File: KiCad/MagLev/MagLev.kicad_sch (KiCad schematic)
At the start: 22 parts, among them Q1 2SD2673, Q2 2SB1708, Q3 2SD2673, Q4 2SB1708, U1 LM324

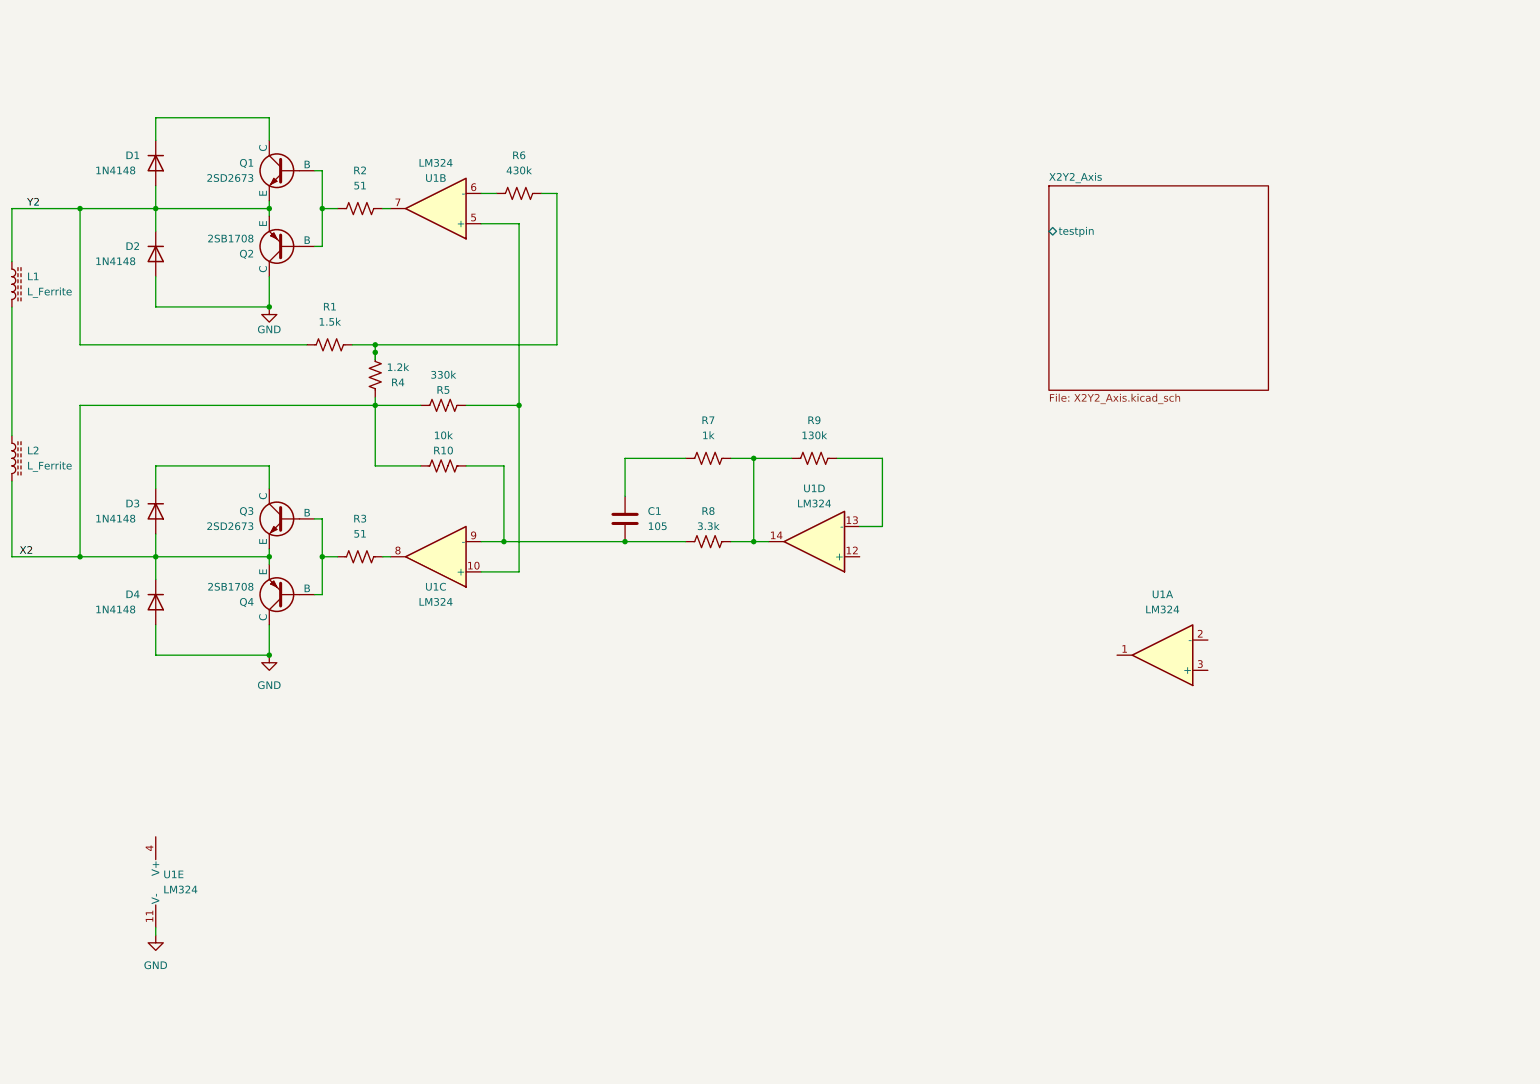
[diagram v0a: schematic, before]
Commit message: Update component names to match ENB schematic.
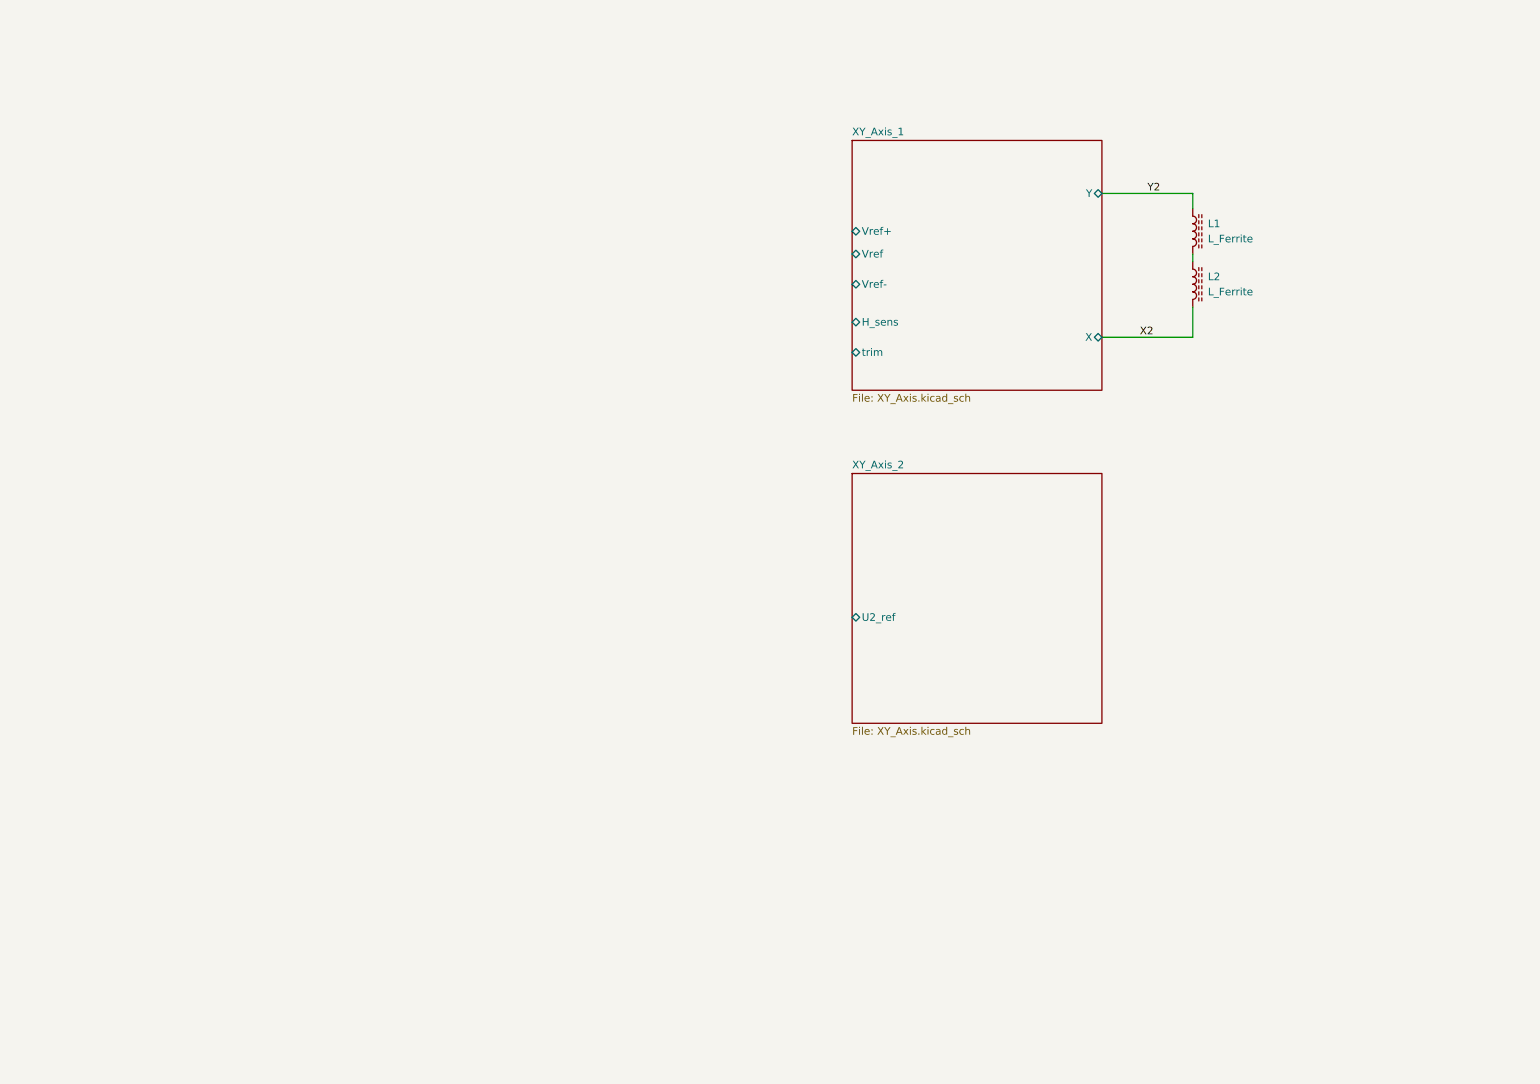
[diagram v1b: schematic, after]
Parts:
- removed C1: 105, symbol Device:C
- removed D1, D2, D3, D4: 1N4148, symbol Device:D
- removed Q1, Q3: 2SD2673, symbol Simulation_SPICE:NPN
- removed Q2, Q4: 2SB1708, symbol Simulation_SPICE:PNP
- removed R1: 1.5k, symbol Device:R_US
- removed R10: 10k, symbol Device:R_US
- removed R2, R3: 51, symbol Device:R_US
- removed R4: 1.2k, symbol Device:R_US
- removed R5: 330k, symbol Device:R_US
- removed R6: 430k, symbol Device:R_US
- removed R7: 1k, symbol Device:R_US
- removed R8: 3.3k, symbol Device:R_US
- removed R9: 130k, symbol Device:R_US
- removed U1: LM324, symbol Amplifier_Operational:LM324
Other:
- removed sheet X2Y2_Axis
- added sheet XY_Axis_1 (XY_Axis.kicad_sch)
- added sheet XY_Axis_2 (XY_Axis.kicad_sch)
- title: (none) -> MagLev

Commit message: Complete schematic equivilant to ENBs.
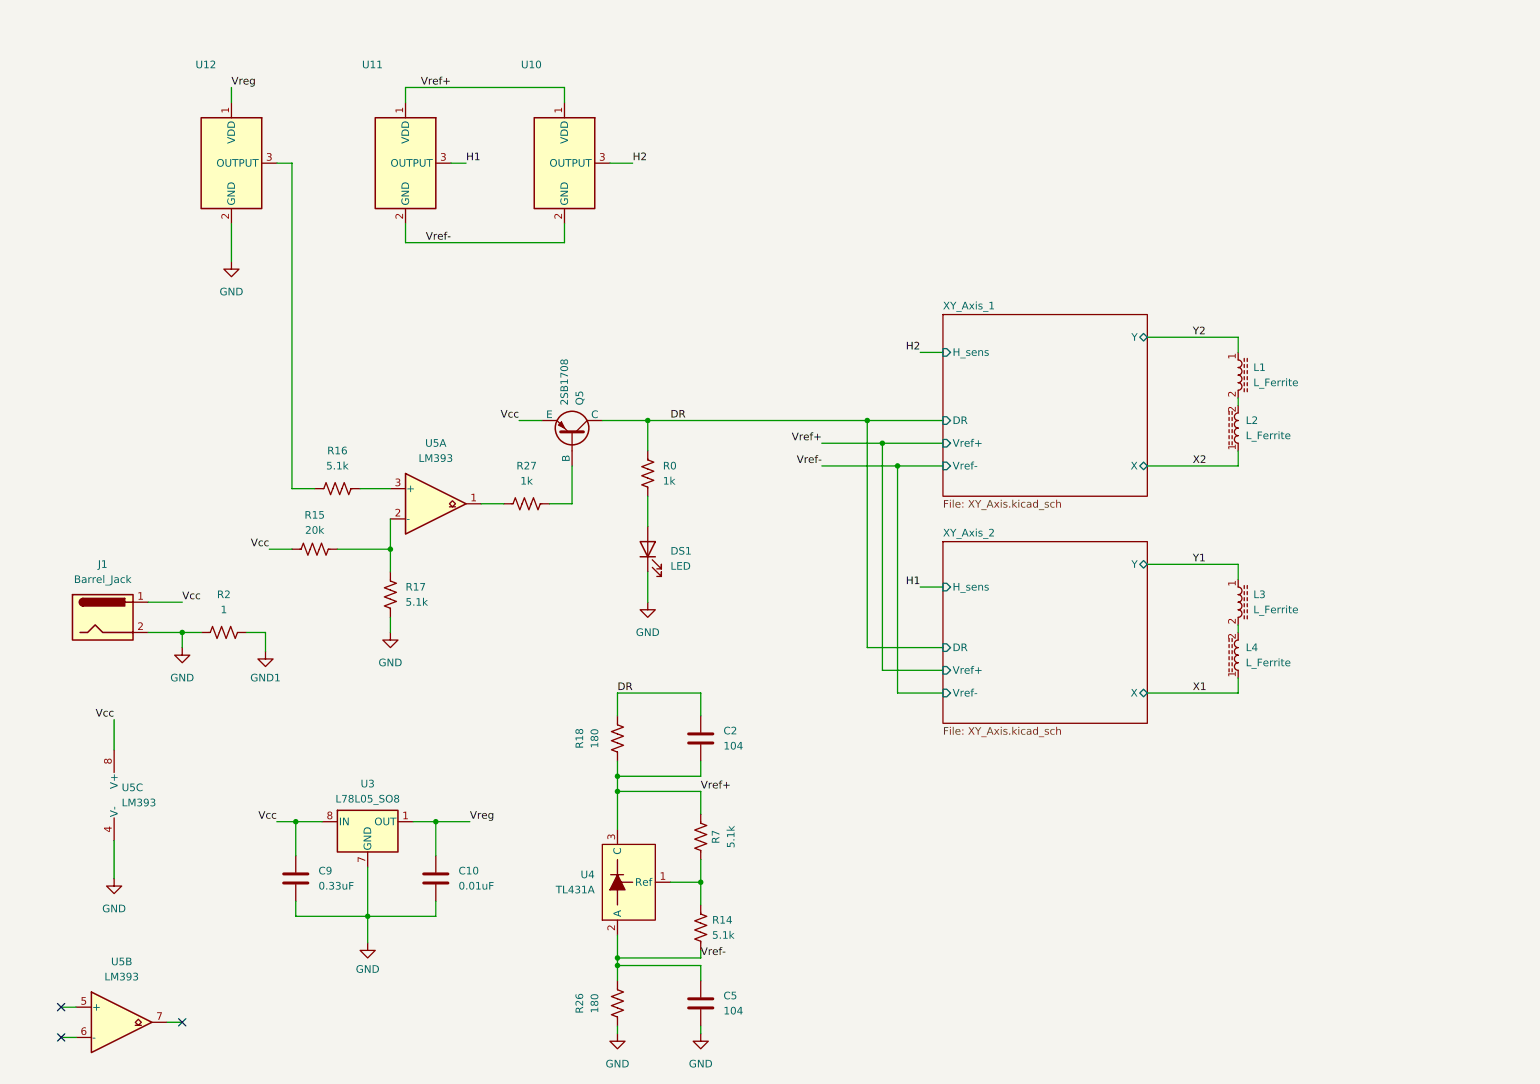
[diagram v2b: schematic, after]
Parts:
- added C10: 0.01uF, symbol Device:C
- added C2, C5: 104, symbol Device:C
- added C9: 0.33uF, symbol Device:C
- added DS1: LED, symbol Device:LED
- added J1: Barrel_Jack, symbol Connector:Barrel_Jack
- added L3, L4: L_Ferrite, symbol Device:L_Ferrite
- added Q5: 2SB1708, symbol Simulation_SPICE:PNP
- added R0, R27: 1k, symbol Device:R_US
- added R14, R16, R17, R7: 5.1k, symbol Device:R_US
- added R15: 20k, symbol Device:R_US
- added R18, R26: 180, symbol Device:R_US
- added R2: 1, symbol Device:R_US
- added U10, U11, U12: ~, symbol Sensor_Magnetic:AH1806-P
- added U3: L78L05_SO8, Package_SO:SOIC-8_3.9x4.9mm_P1.27mm, symbol Regulator_Linear:L78L05_SO8
- added U4: TL431A, symbol MagLev_Library:TL431A
- added U5: LM393, symbol Comparator:LM393
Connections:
- net X2: now also L2.1; no longer L2.2
- net at L1.2: now also L2.2; no longer L2.1
- new net: R14.1, R7.1, U4.1 (Ref)
- new net: R16.2, U12.3 (OUTPUT)
- new net: Q5.2 (B), R27.2
- new net: R27.1, U5.1
- new net: R15.2, R17.1, U5.2 (-)
- new net: R16.1, U5.3 (+)
- new net: DS1.2 (A), R0.2
- new net: L3.2, L4.2
- new net DR: C2.1, Q5.1 (C), R0.1, R18.2
- new net GND: C10.2, C5.2, C9.2, DS1.1 (K), J1.2, R17.2, R2.1, R26.1, U12.2 (GND), U3.2 (GND), U3.3 (GND), U3.6 (GND), U3.7 (GND), U5.4 (V-)
- new net GND1: R2.2
- new net H1: U11.3 (OUTPUT)
- new net H2: U10.3 (OUTPUT)
- new net Vcc: C9.1, J1.1, Q5.3 (E), R15.1, U3.8 (IN), U5.8 (V+)
- new net Vref+: C2.2, R18.1, R7.2, U10.1 (VDD), U11.1 (VDD), U4.3 (C)
- new net Vref-: C5.1, R14.2, R26.2, U10.2 (GND), U11.2 (GND), U4.2 (A)
- new net Vreg: C10.1, U12.1 (VDD), U3.1 (OUT)
- new net X1: L4.1
- new net Y1: L3.1
- no-connect marks 0 -> 3
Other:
- sheet XY_Axis_1 ports: added DR; removed Vref, trim
- sheet XY_Axis_2 ports: added DR, H_sens, Vref+, Vref-, X, Y; removed U2_ref

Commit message: Clean up schematics, add title block info.
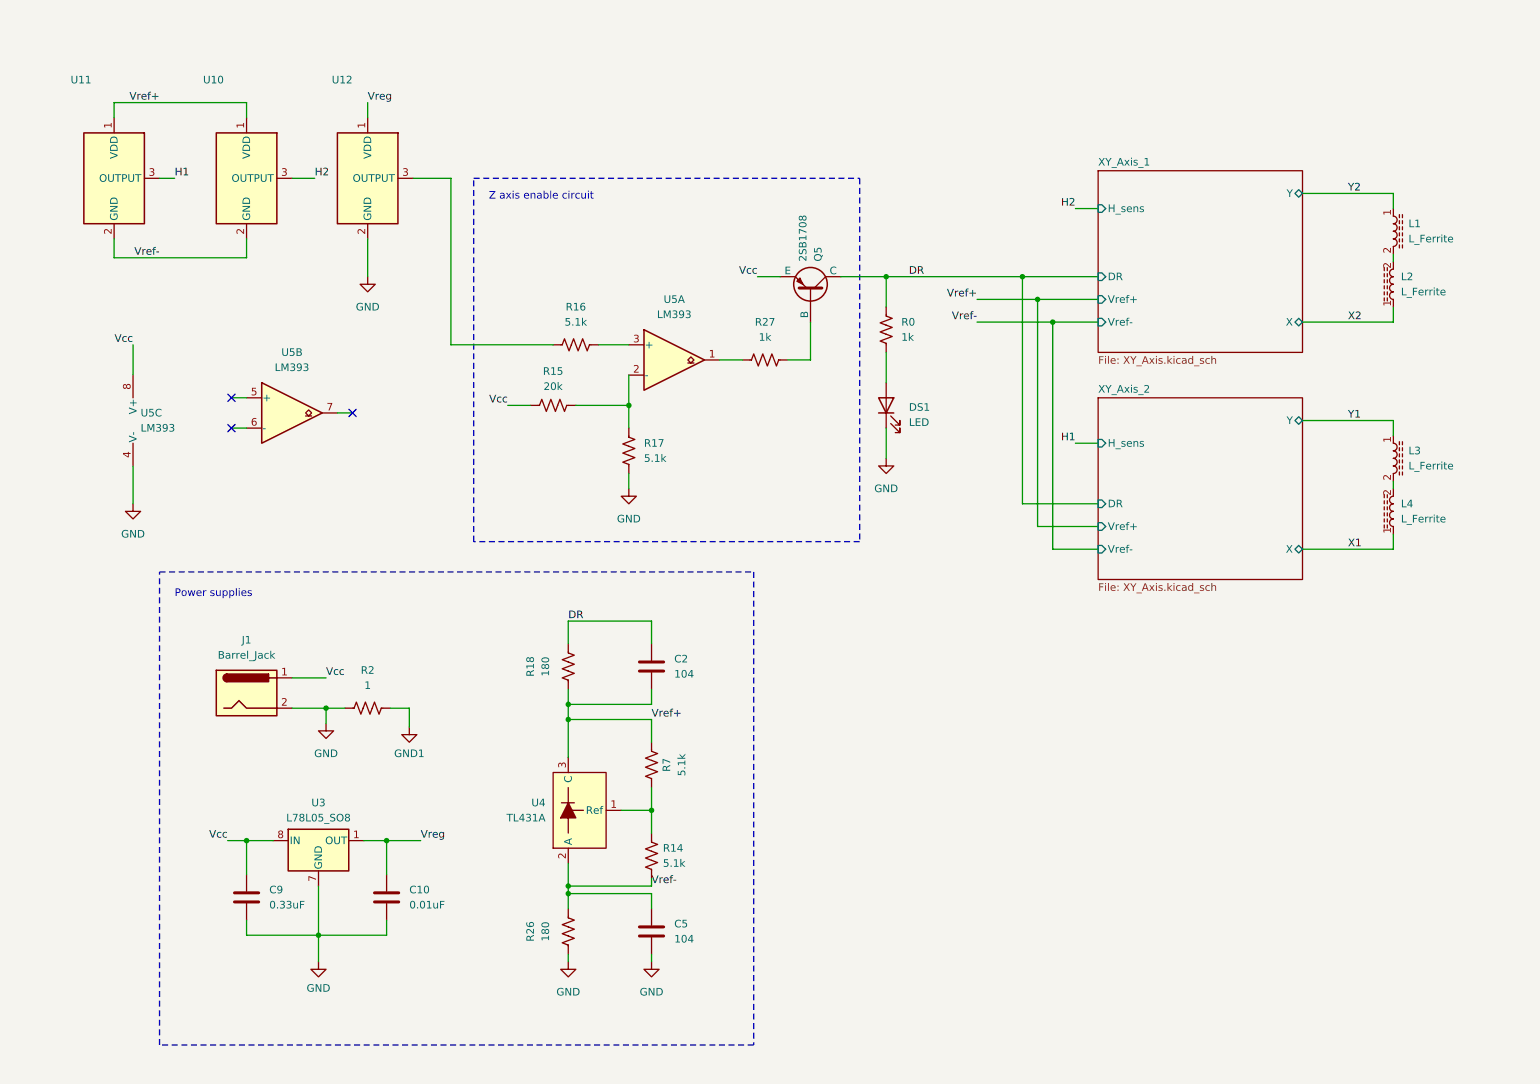
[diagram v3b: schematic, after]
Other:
- note added: "Power supplies"
- note added: "Z axis enable circuit"
- company: (none) -> Kevin Dueck
- moved on the sheet: C10, C2, C5, C9, DS1, J1, L1, L2, L3, L4, Q5, R0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

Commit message: Add footprints to all components, add datasheet directory.
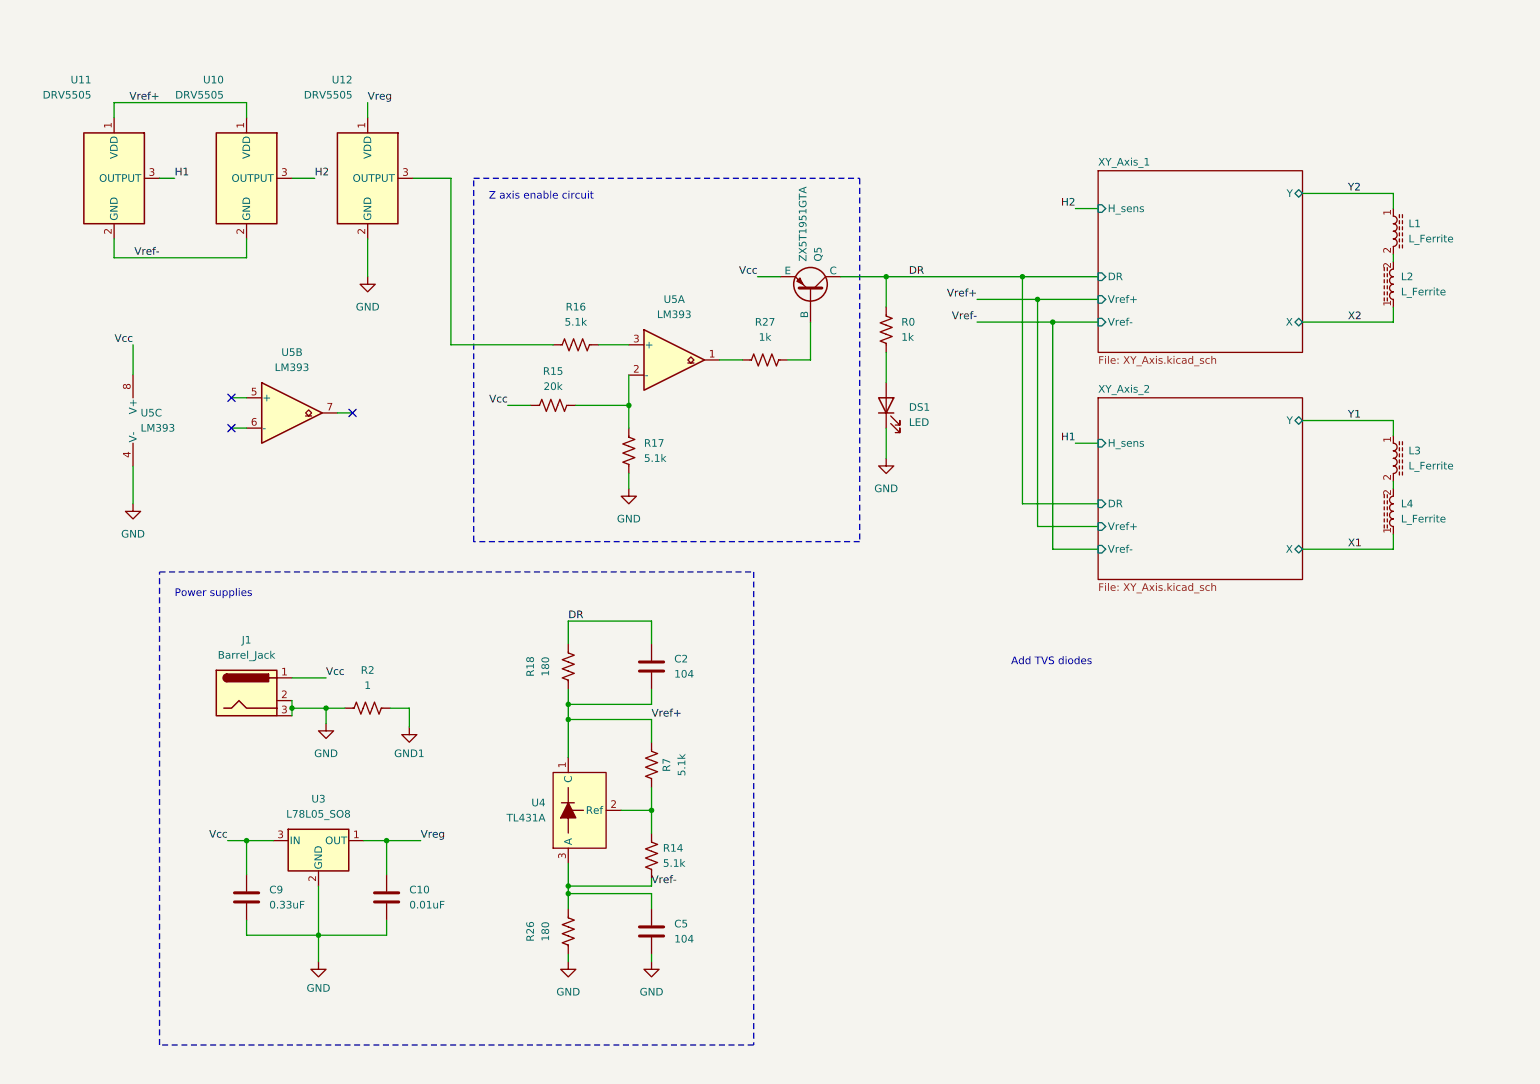
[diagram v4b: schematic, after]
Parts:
- C10, C2, C5, C9: footprint (none) -> Capacitor_SMD:C_0805_2012Metric_Pad1.18x1.45mm_HandSolder
- DS1: footprint (none) -> LED_SMD:LED_0805_2012Metric_Pad1.15x1.40mm_HandSolder
- J1: footprint (none) -> Connector_BarrelJack:BarrelJack_Horizontal
- L1, L2, L3, L4: footprint (none) -> Maglev_Footprint_Library:Maglev_coil
- Q5: value 2SB1708 -> ZX5T1951GTA; footprint (none) -> Maglev_Footprint_Library:SOT-223-3_TabPin2_BJT
- R0, R14, R15, R16, R17, R18, R2, R26, R27, R7: footprint (none) -> Resistor_SMD:R_0805_2012Metric_Pad1.20x1.40mm_HandSolder
- U10, U11, U12: value ~ -> DRV5505; footprint (none) -> Package_TO_SOT_THT:TO-92Flat
- U3: footprint Package_SO:SOIC-8_3.9x4.9mm_P1.27mm -> Maglev_Footprint_Library:SOT-89-3_Handsoldering_Vref
- U4: footprint (none) -> Package_TO_SOT_SMD:SOT-23_Handsoldering
- U5: footprint (none) -> Package_SO:SOIC-8_3.9x4.9mm_P1.27mm
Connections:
- net GND: now also J1.3; no longer U3.3 (GND), U3.6 (GND), U3.7 (GND)
- net Vcc: now also U3.3 (IN); no longer U3.8 (IN)
- net Vref+: now also U4.1 (C); no longer U4.3 (C)
- net Vref-: now also U4.3 (A); no longer U4.2 (A)
- net at R14.1, R7.1: now also U4.2 (Ref); no longer U4.1 (Ref)
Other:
- note added: "Add TVS diodes"
- title: MagLev -> Magnetic Levitation Main Circuit
